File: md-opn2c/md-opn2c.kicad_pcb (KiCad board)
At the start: 2 copper layers, 57.2 x 42.5 mm, 37 parts, among them U1 TL072, U3 74HCT08, U4 YM3438

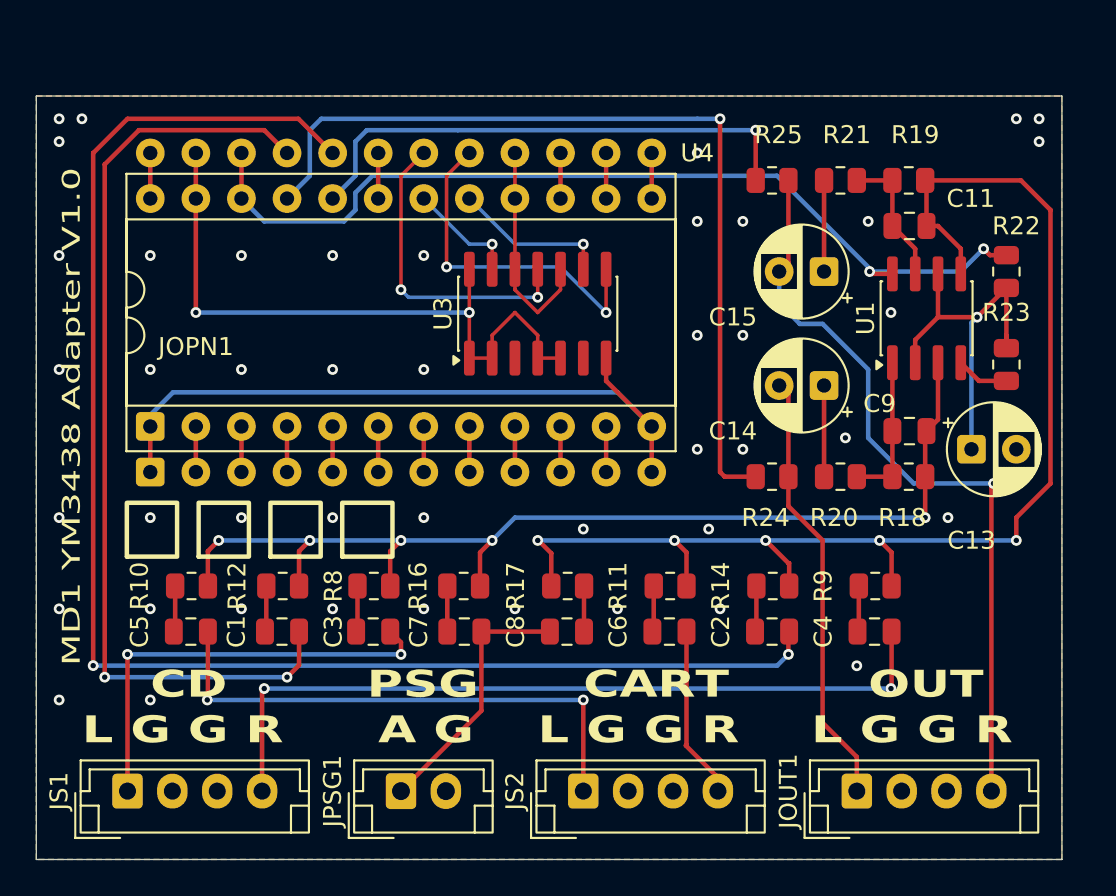
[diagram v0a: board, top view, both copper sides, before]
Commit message: Board rev after testing initial prototype
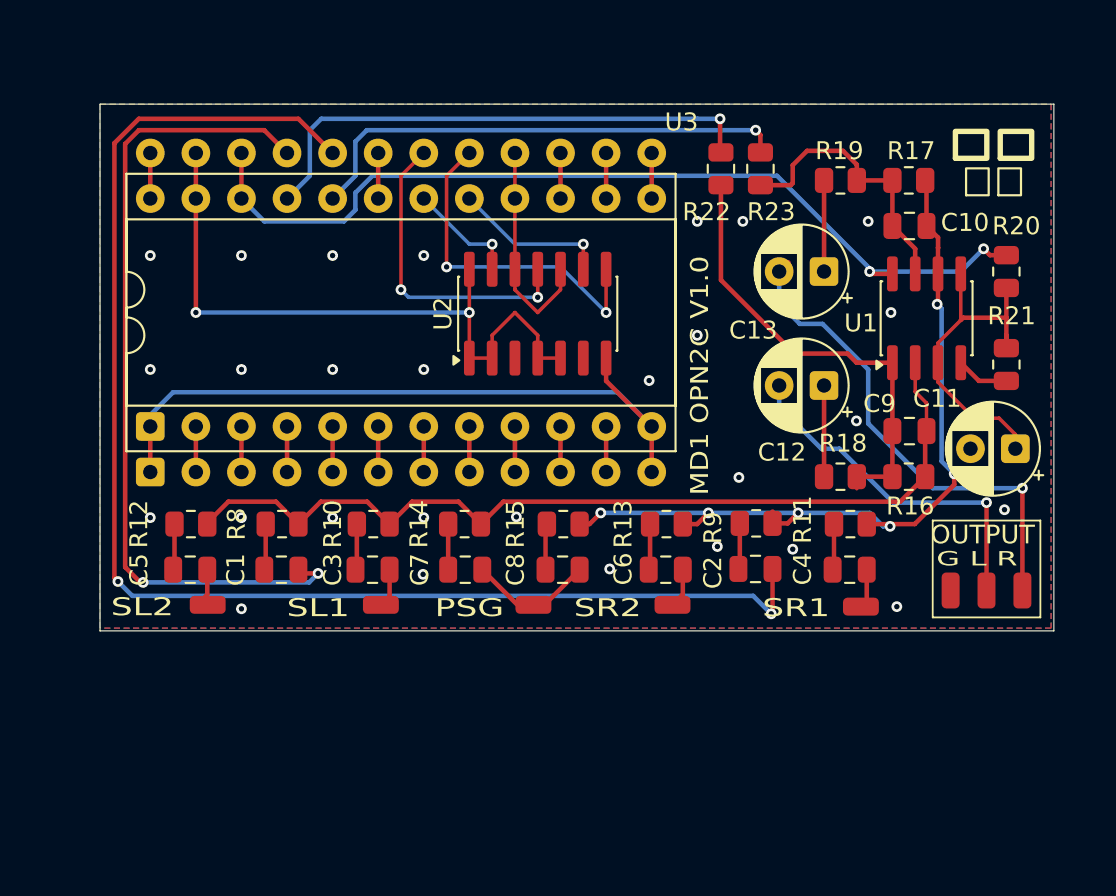
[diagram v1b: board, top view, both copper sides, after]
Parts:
- removed JOUT1, JS1, JS2: Conn_01x04_Pin, Connector_JST:JST_EH_B4B-EH-A_1x04_P2.50mm_Vertical
- removed JPSG1: Conn_01x02_Pin, Connector_JST:JST_EH_B2B-EH-A_1x02_P2.50mm_Vertical
- added IN_PSG1: TestPoint_Small, Connector_Wire:SolderWirePad_1x01_SMD_1x2mm, F.Cu at (46.8, 45.5)
- added IN_SL1: TestPoint_Small, Connector_Wire:SolderWirePad_1x01_SMD_1x2mm, F.Cu at (38.2, 45.5)
- added IN_SL2: TestPoint_Small, Connector_Wire:SolderWirePad_1x01_SMD_1x2mm, F.Cu at (28.6, 45.5)
- added IN_SR1: TestPoint_Small, Connector_Wire:SolderWirePad_1x01_SMD_1x2mm, F.Cu at (65.0, 45.6)
- added IN_SR2: TestPoint_Small, Connector_Wire:SolderWirePad_1x01_SMD_1x2mm, F.Cu at (54.5, 45.5)
- added OUT_GND1: TestPoint_Small, Connector_Wire:SolderWirePad_1x01_SMD_1x2mm, F.Cu at (70.0, 44.7)
- added OUT_L1: TestPoint_Small, Connector_Wire:SolderWirePad_1x01_SMD_1x2mm, F.Cu at (72.0, 44.7)
- added OUT_R1: TestPoint_Small, Connector_Wire:SolderWirePad_1x01_SMD_1x2mm, F.Cu at (74.0, 44.7)
- C3, C4, C5, C6, C7, C8: value 10uF/16V -> 1uF/16V
- R22: renamed from R24; value 10k -> 100k
- R23: renamed from R25; value 10k -> 100k
- moved R22 17.4 mm to (57.2, 21.2), turned to 90 degrees
- moved C4 3.72 mm to (64.4, 43.5)
- moved R11 3.72 mm to (64.4, 41.0)
- moved C2 3.61 mm to (59.1, 43.5)
- moved R9 3.61 mm to (59.2, 41.0)
- moved C8 3.46 mm to (48.4, 43.5), turned to 180 degrees
- moved R15 3.46 mm to (48.4, 41.0), turned to 0 degrees
- moved C6 3.46 mm to (54.1, 43.5)
- moved R13 3.46 mm to (54.2, 41.0)
- moved C7 3.45 mm to (43.0, 43.5)
- moved R14 3.45 mm to (42.9, 41.0)
- moved C1 3.45 mm to (32.7, 43.5)
- moved C3 3.45 mm to (37.8, 43.5)
- moved C5 3.45 mm to (27.6, 43.5)
- moved R10 3.45 mm to (37.8, 41.0)
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- renumbered C11 to C10, C13 to C11, C14 to C12, C15 to C13, R8 to R10, R9 to R11, R10 to R12, R11 to R13, R16 to R14, R17 to R15, R18 to R16, R19 to R17, R20 to R18, R21 to R19, R22 to R20, R23 to R21, R12 to R8, R14 to R9, U3 to U2, U4 to U3
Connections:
- C10 pad 2: Net-(C11-Pad2) -> /BUF_R
- C9 pad 2: Net-(C9-Pad2) -> /BUF_L
- R16 pad 2: Net-(C9-Pad2) -> /BUF_L
- R17 pad 2: Net-(C11-Pad2) -> /BUF_R
- R18 pad 1: Net-(C9-Pad2) -> /BUF_L
- R19 pad 1: Net-(C11-Pad2) -> /BUF_R
- R22 pad 1: /OUT_L -> /BUF_L
- R23 pad 1: /OUT_R -> /BUF_R
- U1 pad 1: Net-(C9-Pad2) -> /BUF_L
- U1 pad 2: /BIAS_2_5V -> /MIX_L
- U1 pad 3: /MIX_L -> /BIAS_2_5V
- U1 pad 5: /MIX_R -> /BIAS_2_5V
- U1 pad 6: /BIAS_2_5V -> /MIX_R
- U1 pad 7: Net-(C11-Pad2) -> /BUF_R
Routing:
- net /SR1: track 43.9 -> 2.19 mm, vias 2 -> 0
- net /SL2: track 29.9 -> 2.20 mm, vias 2 -> 0
- net /MIX_R: track 71.6 -> 45.5 mm, vias 5 -> 6
- net /BUF_L: track 0.00 -> 25.8 mm
- net /SL1: track 24.4 -> 2.16 mm, vias 2 -> 0
- net /ORIG_OUT_L: track 49.2 -> 29.4 mm
- net /BUF_R: track 0.00 -> 15.7 mm
- net /OUT_R: track 42.6 -> 27.8 mm
- net /MIX_L: track 60.0 -> 50.9 mm, vias 5 -> 0
- net Net-(C9-Pad2): track 8.34 -> 0.00 mm
- net Net-(C11-Pad2): track 7.72 -> 0.00 mm
- net /PSG: track 14.6 -> 7.05 mm
- net /SR2: track 9.64 -> 2.20 mm
- net /OPN2C_MOL: track 53.0 -> 46.0 mm
- net /OPN2C_MOR: track 83.8 -> 77.7 mm
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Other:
- board size 57.2 x 42.5 mm -> 53.1 x 29.4 mm
- board text added: "G L R"
- board text added: "MD1 OPN2C V1.0"
- board text added: "OUTPUT"
- board text added: "SL1"
- board text added: "SL2"
- board text added: "SR1"
- board text added: "SR2"
- board text added: "モフ"
- board text added: "電子"
- board text removed: "A G"
- board text removed: "CART"
- board text removed: "CD"
- board text removed: "L G G R"
- board text removed: "MD1 YM3438 Adapter V1.0"
- board text removed: "OUT"
- board text removed: "モフ電子"

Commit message: little tweaks
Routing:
- net VCC: track 37.8 -> 36.8 mm

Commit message: Updated readme, gerbers
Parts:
- moved IN_SR2 1.79 mm to (56.3, 45.6)
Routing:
- net /PSG: track 7.05 -> 11.7 mm, vias 0 -> 2
- net GNDA: vias 28 -> 31
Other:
- board text added: "LINE OUT"
- board text removed: "OUTPUT"

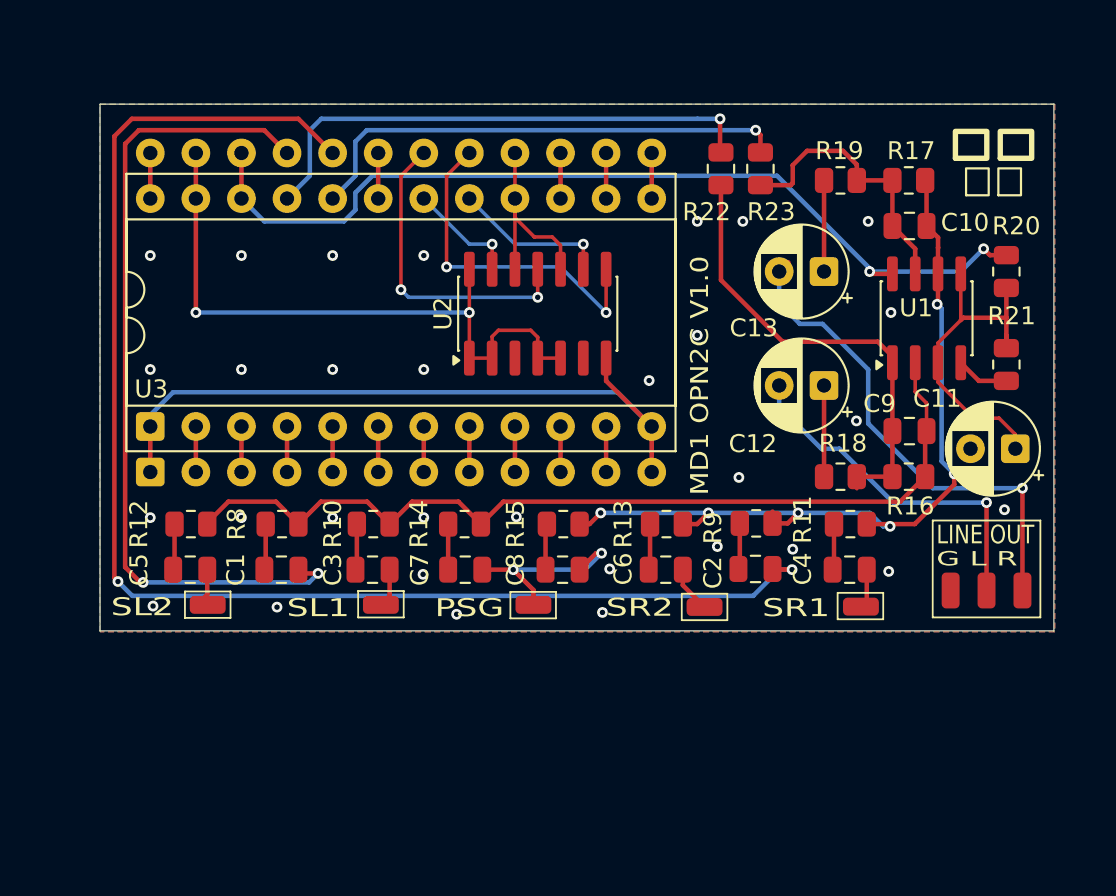
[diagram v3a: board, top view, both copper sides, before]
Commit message: Defaulted filter to ~16KHz, tidied up board
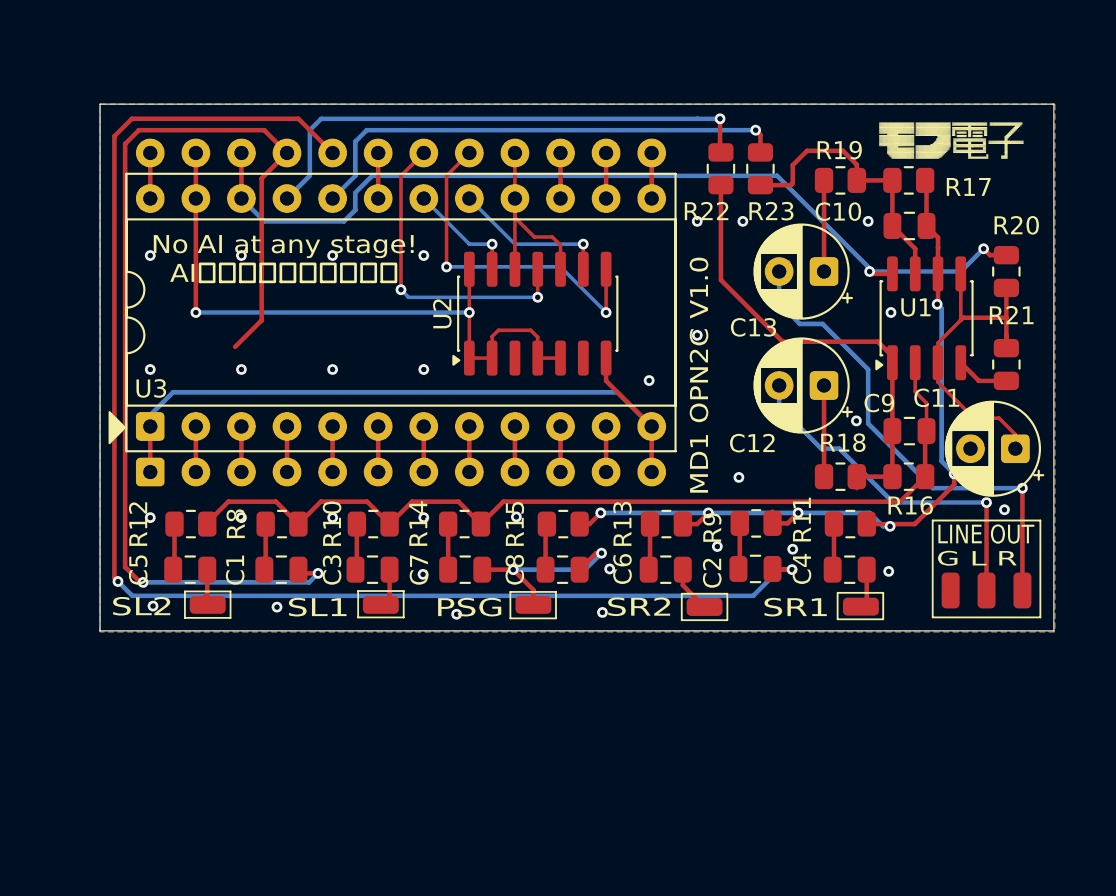
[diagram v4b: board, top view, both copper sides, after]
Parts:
- C10, C9: value 150pF/50V -> 33pF/50V
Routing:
- net /OPN2C_MOL: track 46.0 -> 58.0 mm
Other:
- board text added: "No AI at any stage! AI全く利用していないよ"
- board text removed: "モフ"
- board text removed: "電子"

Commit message: Updated readme for upcoming V1.0.1 revision
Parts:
- added JP1: SolderJumper_3_Open, Jumper:SolderJumper-3_P2.0mm_Open_TrianglePad1.0x1.5mm, B.Cu at (26.7, 41.0)
- added JP2: SolderJumper_3_Open, Jumper:SolderJumper-3_P2.0mm_Open_TrianglePad1.0x1.5mm, B.Cu at (33.1, 41.0)
- added R24: 10k, Resistor_SMD:R_0603_1608Metric, F.Cu at (27.1, 28.9)
- added R25: 10k, Resistor_SMD:R_0603_1608Metric, F.Cu at (30.3, 28.9)
- C1, C10, C2, C3, C4, C5, C6, C7, C8, C9: footprint Capacitor_SMD:C_0805_2012Metric -> Capacitor_SMD:C_0603_1608Metric
- JOPN1: value YM2612 Socket -> DIP24 Header
- R10, R11, R12, R13, R14, R15, R16, R17, R18, R19, R20, R21, R22, R23, R8, R9: footprint Resistor_SMD:R_0805_2012Metric -> Resistor_SMD:R_0603_1608Metric
- U1: value TL072 -> TL972
- moved C2 33.9 mm to (30.3, 25.7)
- moved R12 33.2 mm to (60.6, 37.5), turned to -90 degrees
- moved IN_SL2 32.3 mm to (60.6, 41.3)
- moved C5 32.0 mm to (59.1, 37.5), turned to 90 degrees
- moved R9 32.0 mm to (30.3, 27.3)
- moved R14 27.6 mm to (70.2, 36.8), turned to -90 degrees
- moved C7 26.5 mm to (68.6, 36.8), turned to 90 degrees
- moved C8 25.4 mm to (70.2, 30.5), turned to -90 degrees
- moved R23 25.0 mm to (34.9, 26.2)
- moved OUT_GND1 24.8 mm to (66.4, 20.2), turned to 180 degrees
- moved OUT_L1 24.8 mm to (68.4, 20.2), turned to 180 degrees
- moved OUT_R1 24.8 mm to (70.4, 20.2), turned to 180 degrees
- moved R22 24.7 mm to (33.0, 26.2)
- moved R15 22.7 mm to (68.6, 30.5), turned to 90 degrees
- moved C11 20.2 mm to (60.3, 21.6)
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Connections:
- R8 pad 2: /MIX_L -> Net-(JP1-B)
- R9 pad 2: /MIX_R -> Net-(JP2-B)
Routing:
- net /OPN2C_MOR: track 77.9 -> 8.37 mm, vias 2 -> 0
- net /OPN2C_MOL: track 58.0 -> 9.01 mm, vias 2 -> 1
- net /BUF_R: track 15.7 -> 42.9 mm, vias 0 -> 2
- net /ORIG_OUT_L: track 29.4 -> 2.54 mm, vias 1 -> 0
- net /ORIG_OUT_R: track 27.6 -> 2.80 mm, vias 1 -> 0
- net Net-(JP2-B): track 0.00 -> 20.6 mm, vias 0 -> 1
- net /MIX_R: track 45.5 -> 64.7 mm, vias 6 -> 3
- net /SR1: track 2.19 -> 20.5 mm, vias 0 -> 2
- net /MIX_L: track 50.9 -> 69.1 mm, vias 0 -> 3
- net Net-(JP1-B): track 0.00 -> 17.5 mm, vias 0 -> 1
- net Net-(JP2-A): track 0.00 -> 16.1 mm, vias 0 -> 1
- net Net-(JP1-A): track 0.00 -> 13.9 mm, vias 0 -> 1
- net /BUF_L: track 26.0 -> 38.1 mm, vias 0 -> 2
- net VCC: track 36.8 -> 48.0 mm, vias 2 -> 3
- net VCCA: track 51.6 -> 43.0 mm
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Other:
- board size 53.1 x 29.4 mm -> 48.7 x 23.9 mm
- board text added: "FM音源をここに"
- board text added: "Human-made!! 全くAI利用していません"
- board text added: "Jumpers: YM2612 YM3438"
- board text added: "MD-OPN2C V1.0.1"
- board text removed: "MD1 OPN2C V1.0"
- board text removed: "No AI at any stage! AI全く利用していないよ"

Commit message: Reduced BOM cost by a few bucks
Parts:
- removed JOPN1: DIP24 Header, Package_DIP:DIP-24_W15.24mm
- added J1: Conn_01x12_Pin, Connector_PinHeader_2.54mm:PinHeader_1x12_P2.54mm_Vertical, B.Cu at (25.4, 38.1)
- added J2: Conn_01x12_Pin, Connector_PinHeader_2.54mm:PinHeader_1x12_P2.54mm_Vertical, B.Cu at (25.4, 22.9)
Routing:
- net /MIX_L: track 69.1 -> 69.8 mm
- net GNDA: vias 31 -> 28
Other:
- board text added: "FM音源"
- board text removed: "FM音源をここに"

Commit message: 2.2k pulldowns for YM2612 implemented as optional pads on the underside; note written in README
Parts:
- added R2: 2.2k, Resistor_SMD:R_0805_2012Metric, B.Cu at (27.9, 27.9)
- added R3: 2.2k, Resistor_SMD:R_0805_2012Metric, B.Cu at (30.5, 27.9)
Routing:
- net /OPN2C_MOR: track 8.37 -> 10.8 mm, vias 0 -> 1
- net /OPN2C_MOL: track 9.01 -> 11.3 mm
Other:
- board text added: "YM2612: 2 x 2.2k R"

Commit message: v1.0.2
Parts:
- added JP3: SolderJumper_2_Open, Jumper:SolderJumper-2_P1.3mm_Open_TrianglePad1.0x1.5mm, B.Cu at (27.9, 26.7)
- added JP4: SolderJumper_2_Open, Jumper:SolderJumper-2_P1.3mm_Open_TrianglePad1.0x1.5mm, B.Cu at (30.5, 26.7)
- moved R2 2.54 mm to (27.9, 30.5)
- moved R3 2.54 mm to (30.5, 30.5)
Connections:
- R2 pad 1: /OPN2C_MOL -> Net-(JP3-A)
- R3 pad 1: /OPN2C_MOR -> Net-(JP4-A)
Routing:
- net Net-(JP4-A): track 0.00 -> 2.17 mm
- net Net-(JP3-A): track 0.00 -> 2.17 mm
- net /OPN2C_MOR: track 10.8 -> 9.76 mm
- net /OPN2C_MOL: track 11.3 -> 10.2 mm
- net GNDA: vias 28 -> 26
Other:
- board text added: "MD-OPN2C V1.0.2"
- board text removed: "MD-OPN2C V1.0.1"
- board text removed: "YM2612: 2 x 2.2k R"
